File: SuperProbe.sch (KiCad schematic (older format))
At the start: 66 parts, among them J1 Conn_01x01, J10 Conn_01x01, J11 Conn_01x01, J12 Conn_01x01, J13 Conn_01x01, J14 Conn_01x01, J15 Conn_01x01, J16 Conn_01x01, J17 Conn_01x02, J2 Conn_01x01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

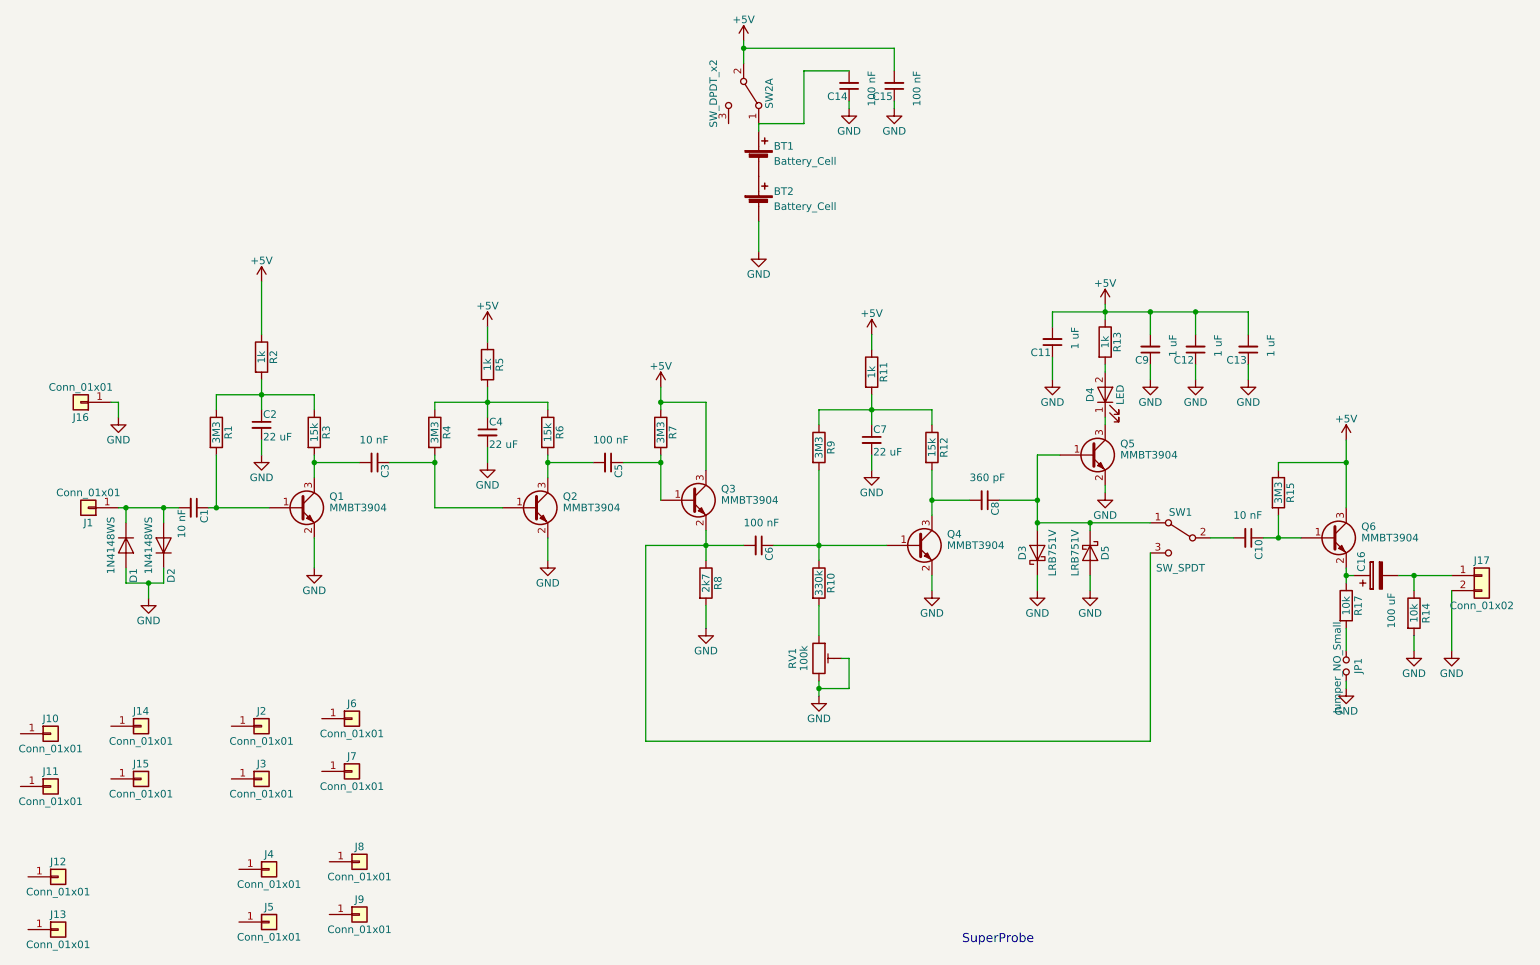
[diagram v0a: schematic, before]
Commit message: Uses 9 volt battery and board shrink
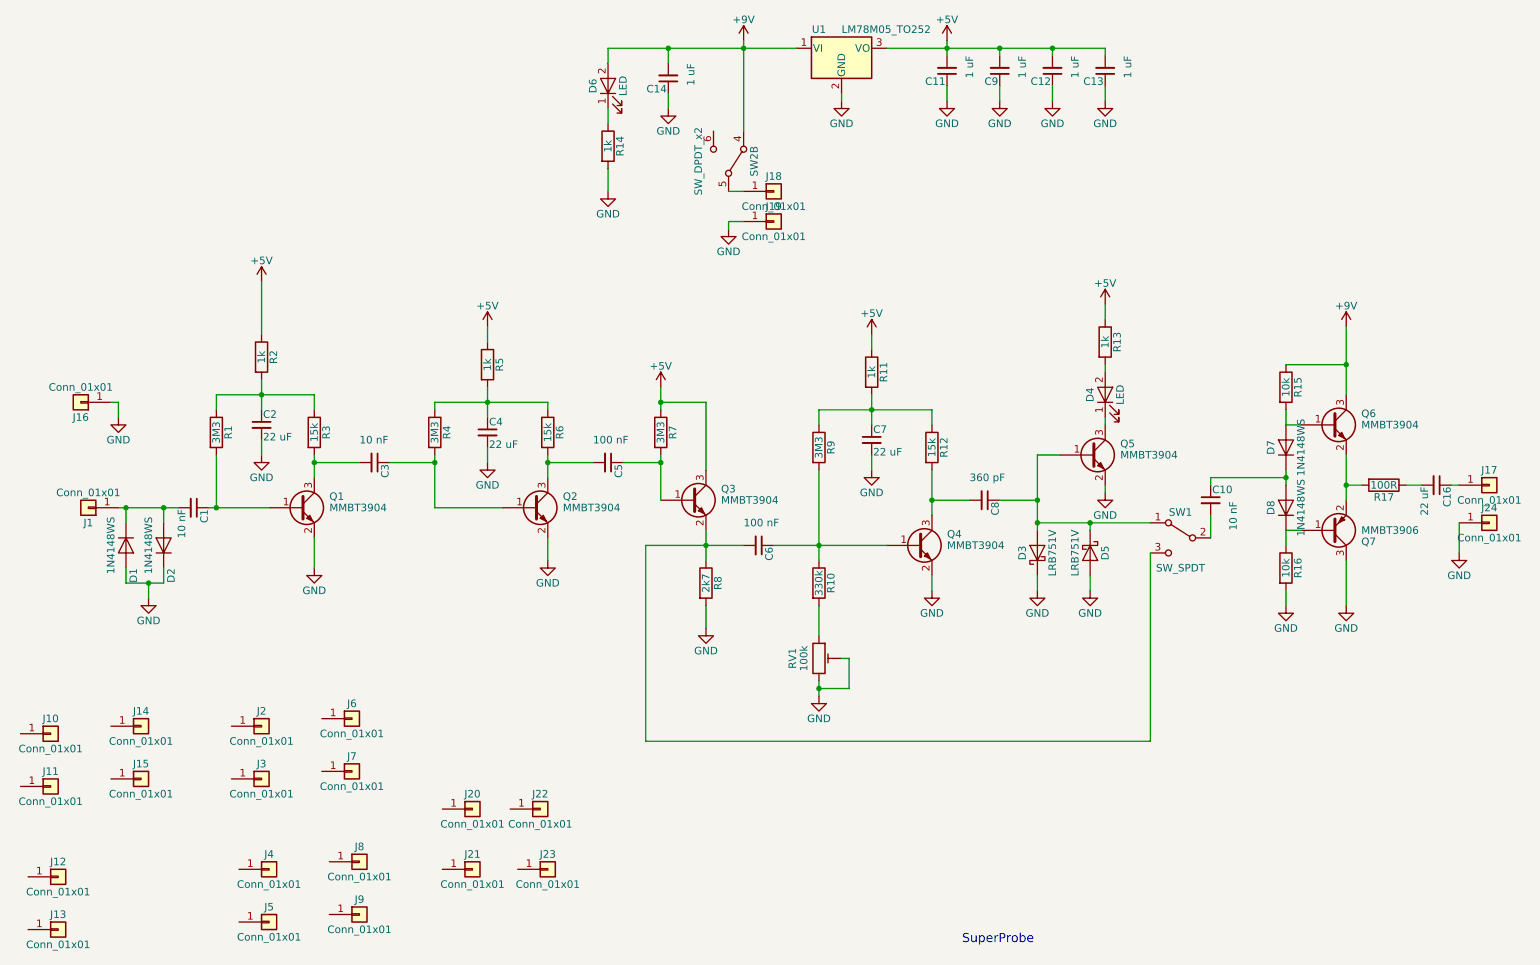
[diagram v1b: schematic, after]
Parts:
- removed BT1, BT2: Battery_Cell, Battery_Holders:Keystone_103_1x20mm-CoinCell, symbol Battery_Cell
- removed C14: 100 nF, Capacitors_SMD:C_0805_HandSoldering, symbol C_Small
- removed C16: 100 uF, Capacitors_SMD:CP_Elec_5x5.3, symbol CP
- removed J17: Conn_01x02, Connectors_Terminal_Blocks:TerminalBlock_bornier-2_P5.08mm, symbol Conn_01x02
- removed JP1: Jumper_NO_Small, Pin_Headers:Pin_Header_Straight_1x02_Pitch2.54mm, symbol Jumper_NO_Small
- removed SW2: SW_DPDT_x2, SuperProbe:DPDTsmallswitch, symbol SW_DPDT_x2
- added C16: 22 uF, Capacitors_SMD:C_1210_HandSoldering, symbol C_Small
- added D6: LED, LEDs:LED_0805_HandSoldering, symbol LED
- added D7, D8: 1N4148WS, Diodes_SMD:D_SOD-323, symbol D
- added J17, J18, J19, J24: Conn_01x01, Connectors:1pin, symbol Conn_01x01
- added J20, J21, J22, J23: Conn_01x01, SuperProbe:BigSlot, symbol Conn_01x01
- added Q7: MMBT3906, TO_SOT_Packages_SMD:SOT-23, symbol MMBT3906
- added R16: 10k, Resistors_SMD:R_0805_HandSoldering, symbol R
- added SW2: SW_DPDT_x2, SuperProbe:DPDTsmallswitch, symbol SW_DPDT_x2
- added U1: LM78M05_TO252, TO_SOT_Packages_SMD:TO-252-3_TabPin2, symbol LM78M05_TO252
- C14: renamed from C15; value 100 nF -> 1 uF
- R14: value 10k -> 1k
- R15: value 3M3 -> 10k
- R17: value 10k -> 100R
- SW1: footprint Pin_Headers:Pin_Header_Straight_1x03_Pitch2.54mm -> SuperProbe:DPDTsmallswitch
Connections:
- net +5V: now also U1.3 (VO); no longer C14.2, Q6.3 (C), R15.1
- net GND: now also J19.1 (Pin_1), J24.1 (Pin_1), Q7.3 (C), R16.2, U1.2 (GND)
- net at Q6.1 (B), R15.2: now also D7.2 (A); no longer C10.1
- net at Q6.2 (E): now also R17.2, Q7.2 (E); no longer R17.1
- net at R14.1: now also D6.1 (K)
- new net: C10.1, D7.1 (K), D8.2 (A)
- new net: J18.1 (Pin_1), SW2.5 (B)
- new net: C16.1, J17.1 (Pin_1)
- new net: C16.2, R17.1
- new net: D8.1 (K), Q7.1 (B), R16.1
- new net +9V: C14.2, D6.2 (A), Q6.3 (C), R15.1, SW2.4 (A), U1.1 (VI)
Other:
- moved on the sheet: C10, C11, C12, C13, C14, C9, Q6

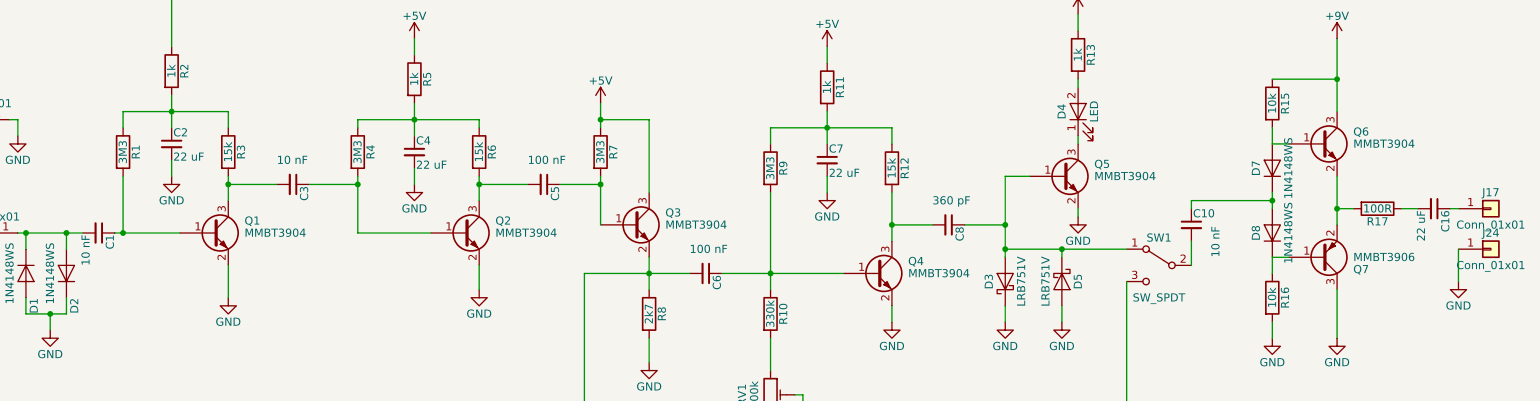
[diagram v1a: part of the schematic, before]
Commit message: Cleaned up the board slightly
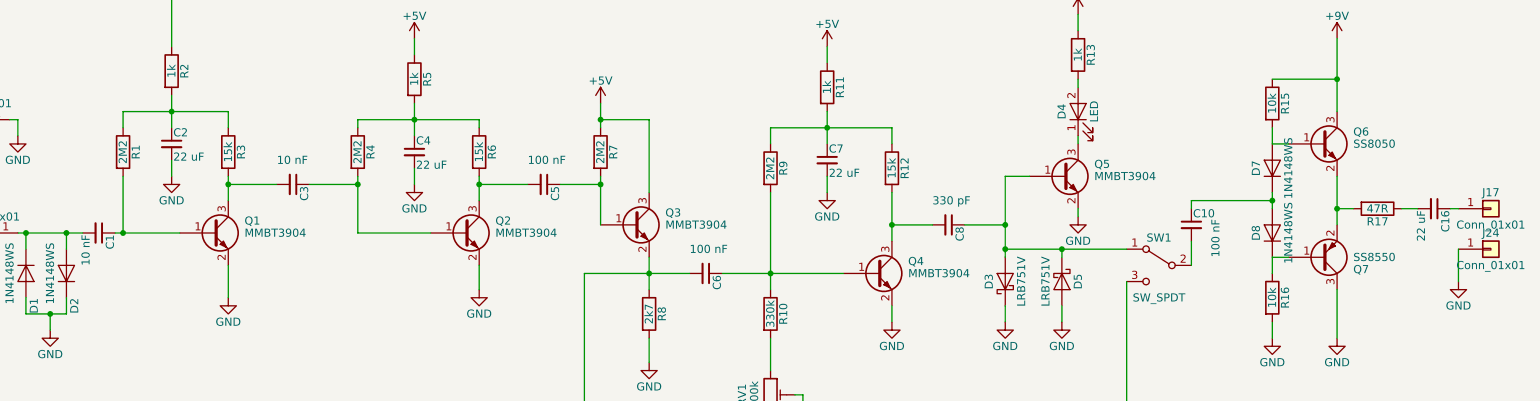
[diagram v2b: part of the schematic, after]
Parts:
- C1, C3: LCSC (none) -> C1710
- C10: value 10 nF -> 100 nF; LCSC (none) -> C49678
- C11, C12, C13, C14, C9: LCSC (none) -> C28323
- C16, C2, C4, C7: footprint Capacitors_SMD:C_1210_HandSoldering -> Capacitors_SMD:C_0805_HandSoldering; LCSC (none) -> C45783
- C5: LCSC (none) -> C49678
- C8: value 360 pF -> 330 pF; LCSC (none) -> C51207
- D1, D2, D7, D8: LCSC (none) -> C2128
- D3, D5: LCSC (none) -> C131730
- D4: LCSC (none) -> C34499
- D6: LCSC (none) -> C2296
- J1, J16, J17, J18, J19, J24: footprint Connectors:1pin -> SuperProbe:PadHole
- Q1, Q2, Q3, Q4, Q5: LCSC (none) -> C20526
- Q6: value MMBT3904 -> SS8050; LCSC (none) -> C2150
- Q7: value MMBT3906 -> SS8550; LCSC (none) -> C8542
- R1, R4, R7, R9: value 3M3 -> 2M2; LCSC (none) -> C26113
- R10: LCSC (none) -> C17629
- R11, R13, R14, R2, R5: LCSC (none) -> C17513
- R12, R3, R6: LCSC (none) -> C17475
- R15, R16: LCSC (none) -> C17414
- R17: value 100R -> 47R; LCSC (none) -> C17714
- U1: LCSC (none) -> C58069

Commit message: Eliminated unneeded diode
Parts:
- removed D3: LRB751V, Diodes_SMD:D_SOD-323_HandSoldering, symbol D_Schottky
- R17: value 47R -> 0R; LCSC C17714 -> C17477
- R8: LCSC (none) -> C17530
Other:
- moved on the sheet: D5
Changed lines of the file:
@@
 $EndComp
 $Comp
-L GND #PWR5
+L GND #PWR01
 U 1 1 5E9B90E6
 P 3200 4300
-F 0 "#PWR5" H 3200 4050 50  0001 C CNN
+F 0 "#PWR01" H 3200 4050 50  0001 C CNN
 F 1 "GND" H 3200 4150 50  0000 C CNN
 F 2 "" H 3200 4300 50  0001 C CNN
@@
 $EndComp
 $Comp
-L GND #PWR4
+L GND #PWR02
 U 1 1 5E9B912A
 P 2850 3550
-F 0 "#PWR4" H 2850 3300 50  0001 C CNN
+F 0 "#PWR02" H 2850 3300 50  0001 C CNN
 F 1 "GND" H 2850 3400 50  0000 C CNN
 F 2 "" H 2850 3550 50  0001 C CNN
@@
 $EndComp
 $Comp
-L +5V #PWR3
+L +5V #PWR03
 U 1 1 5E9B9267
 P 2850 2400
-F 0 "#PWR3" H 2850 2250 50  0001 C CNN
+F 0 "#PWR03" H 2850 2250 50  0001 C CNN
 F 1 "+5V" H 2850 2540 50  0000 C CNN
 F 2 "" H 2850 2400 50  0001 C CNN
@@
 $EndComp
 $Comp
-L GND #PWR8
+L GND #PWR04
 U 1 1 5E9B935A
 P 4750 4250
-F 0 "#PWR8" H 4750 4000 50  0001 C CNN
+F 0 "#PWR04" H 4750 4000 50  0001 C CNN
 F 1 "GND" H 4750 4100 50  0000 C CNN
 F 2 "" H 4750 4250 50  0001 C CNN
@@
 $EndComp
 $Comp
-L GND #PWR7
+L GND #PWR05
 U 1 1 5E9B968B
 P 4350 3600
-F 0 "#PWR7" H 4350 3350 50  0001 C CNN
+F 0 "#PWR05" H 4350 3350 50  0001 C CNN
 F 1 "GND" H 4350 3450 50  0000 C CNN
 F 2 "" H 4350 3600 50  0001 C CNN
@@
 $EndComp
 $Comp
-L +5V #PWR6
+L +5V #PWR06
 U 1 1 5E9B97C5
 P 4350 2700
-F 0 "#PWR6" H 4350 2550 50  0001 C CNN
+F 0 "#PWR06" H 4350 2550 50  0001 C CNN
 F 1 "+5V" H 4350 2840 50  0000 C CNN
 F 2 "" H 4350 2700 50  0001 C CNN
@@
 $EndComp
 $Comp
-L +5V #PWR10
+L +5V #PWR07
 U 1 1 5E9B9BD0
 P 5500 3100
-F 0 "#PWR10" H 5500 2950 50  0001 C CNN
+F 0 "#PWR07" H 5500 2950 50  0001 C CNN
 F 1 "+5V" H 5500 3240 50  0000 C CNN
 F 2 "" H 5500 3100 50  0001 C CNN
@@
 F 2 "Resistors_SMD:R_0805_HandSoldering" V 5730 4400 50  0001 C CNN
 F 3 "" H 5800 4400 50  0001 C CNN
+F 4 "C17530" V 5800 4400 60  0001 C CNN "LCSC"
 	1    5800 4400
 	1    0    0    -1
 $EndComp
 $Comp
-L GND #PWR12
+L GND #PWR08
 U 1 1 5E9B9E9B
 P 5800 4700
-F 0 "#PWR12" H 5800 4450 50  0001 C CNN
+F 0 "#PWR08" H 5800 4450 50  0001 C CNN
 F 1 "GND" H 5800 4550 50  0000 C CNN
 F 2 "" H 5800 4700 50  0001 C CNN
@@
 $EndComp
 $Comp
-L GND #PWR15
+L GND #PWR09
 U 1 1 5E9BA341
 P 6550 5150
-F 0 "#PWR15" H 6550 4900 50  0001 C CNN
+F 0 "#PWR09" H 6550 4900 50  0001 C CNN
 F 1 "GND" H 6550 5000 50  0000 C CNN
 F 2 "" H 6550 5150 50  0001 C CNN
@@
 $EndComp
 $Comp
-L GND #PWR18
+L GND #PWR010
 U 1 1 5E9BA5EE
 P 6900 3650
-F 0 "#PWR18" H 6900 3400 50  0001 C CNN
+F 0 "#PWR010" H 6900 3400 50  0001 C CNN
 F 1 "GND" H 6900 3500 50  0000 C CNN
 F 2 "" H 6900 3650 50  0001 C CNN
@@
 $EndComp
 $Comp
-L +5V #PWR17
+L +5V #PWR011
 U 1 1 5E9BA9B5
 P 6900 2750
-F 0 "#PWR17" H 6900 2600 50  0001 C CNN
+F 0 "#PWR011" H 6900 2600 50  0001 C CNN
 F 1 "+5V" H 6900 2890 50  0000 C CNN
 F 2 "" H 6900 2750 50  0001 C CNN
@@
 $EndComp
 $Comp
-L GND #PWR19
+L GND #PWR012
 U 1 1 5E9BACE0
 P 7300 4450
-F 0 "#PWR19" H 7300 4200 50  0001 C CNN
+F 0 "#PWR012" H 7300 4200 50  0001 C CNN
 F 1 "GND" H 7300 4300 50  0000 C CNN
 F 2 "" H 7300 4450 50  0001 C CNN
@@
 $EndComp
 $Comp
-L D_Schottky D3
-U 1 1 5E9BB050
-P 8000 4200
-F 0 "D3" H 8000 4300 50  0000 C CNN
-F 1 "LRB751V" H 8000 4100 50  0000 C CNN
-F 2 "Diodes_SMD:D_SOD-323_HandSoldering" H 8000 4200 50  0001 C CNN
-F 3 "" H 8000 4200 50  0001 C CNN
-F 4 "C131730" H 8000 4200 60  0001 C CNN "LCSC"
-	1    8000 4200
-	0    -1   -1   0
-$EndComp
-$Comp
-L GND #PWR23
-U 1 1 5E9BB166
-P 8000 4450
-F 0 "#PWR23" H 8000 4200 50  0001 C CNN
-F 1 "GND" H 8000 4300 50  0000 C CNN
-F 2 "" H 8000 4450 50  0001 C CNN
-F 3 "" H 8000 4450 50  0001 C CNN
-	1    8000 4450
-	1    0    0    -1
-$EndComp
-$Comp
 L MMBT3904 Q5
 U 1 1 5E9BB277
@@
 $EndComp
 $Comp
-L GND #PWR28
+L GND #PWR013
 U 1 1 5E9BB380
 P 8450 3800
-F 0 "#PWR28" H 8450 3550 50  0001 C CNN
+F 0 "#PWR013" H 8450 3550 50  0001 C CNN
 F 1 "GND" H 8450 3650 50  0000 C CNN
 F 2 "" H 8450 3800 50  0001 C CNN
@@
 $EndComp
 $Comp
-L +5V #PWR27
+L +5V #PWR014
 U 1 1 5E9BB7DB
 P 8450 2550
-F 0 "#PWR27" H 8450 2400 50  0001 C CNN
+F 0 "#PWR014" H 8450 2400 50  0001 C CNN
 F 1 "+5V" H 8450 2690 50  0000 C CNN
 F 2 "" H 8450 2550 50  0001 C CNN
@@
 $EndComp
 $Comp
-L GND #PWR31
+L GND #PWR015
 U 1 1 5E9BD546
 P 10050 4550
-F 0 "#PWR31" H 10050 4300 50  0001 C CNN
+F 0 "#PWR015" H 10050 4300 50  0001 C CNN
 F 1 "GND" H 10050 4400 50  0000 C CNN
 F 2 "" H 10050 4550 50  0001 C CNN
@@
 $EndComp
 $Comp
-L GND #PWR2
+L GND #PWR016
 U 1 1 5E9BF682
 P 2100 4500
-F 0 "#PWR2" H 2100 4250 50  0001 C CNN
+F 0 "#PWR016" H 2100 4250 50  0001 C CNN
 F 1 "GND" H 2100 4350 50  0000 C CNN
 F 2 "" H 2100 4500 50  0001 C CNN
@@
 $EndComp
 $Comp
-L GND #PWR13
+L GND #PWR017
 U 1 1 5E9C1122
 P 5950 2050
-F 0 "#PWR13" H 5950 1800 50  0001 C CNN
+F 0 "#PWR017" H 5950 1800 50  0001 C CNN
 F 1 "GND" H 5950 1900 50  0000 C CNN
 F 2 "" H 5950 2050 50  0001 C CNN
@@
 $EndComp
 $Comp
-L GND #PWR1
+L GND #PWR018
 U 1 1 5E9C57D4
 P 1900 3300
-F 0 "#PWR1" H 1900 3050 50  0001 C CNN
+F 0 "#PWR018" H 1900 3050 50  0001 C CNN
 F 1 "GND" H 1900 3150 50  0000 C CNN
 F 2 "" H 1900 3300 50  0001 C CNN
@@
 L D_Schottky D5
 U 1 1 5E9C8115
-P 8350 4200
-F 0 "D5" H 8350 4300 50  0000 C CNN
-F 1 "LRB751V" H 8350 4100 50  0000 C CNN
-F 2 "Diodes_SMD:D_SOD-323_HandSoldering" H 8350 4200 50  0001 C CNN
-F 3 "" H 8350 4200 50  0001 C CNN
-F 4 "C131730" H 8350 4200 60  0001 C CNN "LCSC"
-	1    8350 4200
+P 8000 4200
+F 0 "D5" H 8000 4300 50  0000 C CNN
+F 1 "LRB751V" H 8000 4100 50  0000 C CNN
+F 2 "Diodes_SMD:D_SOD-323_HandSoldering" H 8000 4200 50  0001 C CNN
+F 3 "" H 8000 4200 50  0001 C CNN
+F 4 "C131730" H 8000 4200 60  0001 C CNN "LCSC"
+	1    8000 4200
 	0    1    1    0
 $EndComp
 $Comp
-L GND #PWR25
+L GND #PWR019
 U 1 1 5E9C8204
-P 8350 4450
-F 0 "#PWR25" H 8350 4200 50  0001 C CNN
-F 1 "GND" H 8350 4300 50  0000 C CNN
-F 2 "" H 8350 4450 50  0001 C CNN
-F 3 "" H 8350 4450 50  0001 C CNN
-	1    8350 4450
+P 8000 4450
+F 0 "#PWR019" H 8000 4200 50  0001 C CNN
+F 1 "GND" H 8000 4300 50  0000 C CNN
+F 2 "" H 8000 4450 50  0001 C CNN
+F 3 "" H 8000 4450 50  0001 C CNN
+	1    8000 4450
 	1    0    0    -1
 $EndComp
@@
 $EndComp
 $Comp
-L +9V #PWR30
+L +9V #PWR020
 U 1 1 5E9C8FE7
 P 10050 2700
-F 0 "#PWR30" H 10050 2550 50  0001 C CNN
+F 0 "#PWR020" H 10050 2550 50  0001 C CNN
 F 1 "+9V" H 10050 2840 50  0000 C CNN
 F 2 "" H 10050 2700 50  0001 C CNN
@@
 $EndComp
 $Comp
-L +9V #PWR14
+L +9V #PWR021
 U 1 1 5E9C9102
 P 6050 800
-F 0 "#PWR14" H 6050 650 50  0001 C CNN
+F 0 "#PWR021" H 6050 650 50  0001 C CNN
 F 1 "+9V" H 6050 940 50  0000 C CNN
 F 2 "" H 6050 800 50  0001 C CNN
@@
 $EndComp
 $Comp
-L GND #PWR11
+L GND #PWR022
 U 1 1 5E9C9570
 P 5550 1250
-F 0 "#PWR11" H 5550 1000 50  0001 C CNN
+F 0 "#PWR022" H 5550 1000 50  0001 C CNN
 F 1 "GND" H 5550 1100 50  0000 C CNN
 F 2 "" H 5550 1250 50  0001 C CNN
@@
 $EndComp
 $Comp
-L GND #PWR16
+L GND #PWR023
 U 1 1 5E9CAB9C
 P 6700 1200
-F 0 "#PWR16" H 6700 950 50  0001 C CNN
+F 0 "#PWR023" H 6700 950 50  0001 C CNN
 F 1 "GND" H 6700 1050 50  0000 C CNN
 F 2 "" H 6700 1200 50  0001 C CNN
@@
 $EndComp
 $Comp
-L +5V #PWR20
+L +5V #PWR024
 U 1 1 5E9CAFF7
 P 7400 800
-F 0 "#PWR20" H 7400 650 50  0001 C CNN
+F 0 "#PWR024" H 7400 650 50  0001 C CNN
 F 1 "+5V" H 7400 940 50  0000 C CNN
 F 2 "" H 7400 800 50  0001 C CNN
@@
 $EndComp
 $Comp
-L GND #PWR21
+L GND #PWR025
 U 1 1 5E9CB8EC
 P 7400 1200
-F 0 "#PWR21" H 7400 950 50  0001 C CNN
+F 0 "#PWR025" H 7400 950 50  0001 C CNN
 F 1 "GND" H 7400 1050 50  0000 C CNN
 F 2 "" H 7400 1200 50  0001 C CNN
@@
 $EndComp
 $Comp
-L GND #PWR22
+L GND #PWR026
 U 1 1 5E9CB9C3
 P 7750 1200
-F 0 "#PWR22" H 7750 950 50  0001 C CNN
+F 0 "#PWR026" H 7750 950 50  0001 C CNN
 F 1 "GND" H 7750 1050 50  0000 C CNN
 F 2 "" H 7750 1200 50  0001 C CNN
@@
 $EndComp
 $Comp
-L GND #PWR24
+L GND #PWR027
 U 1 1 5E9CBA9A
 P 8100 1200
-F 0 "#PWR24" H 8100 950 50  0001 C CNN
+F 0 "#PWR027" H 8100 950 50  0001 C CNN
 F 1 "GND" H 8100 1050 50  0000 C CNN
 F 2 "" H 8100 1200 50  0001 C CNN
@@
 $EndComp
 $Comp
-L GND #PWR26
+L GND #PWR028
 U 1 1 5E9CBEDE
 P 8450 1200
-F 0 "#PWR26" H 8450 950 50  0001 C CNN
+F 0 "#PWR028" H 8450 950 50  0001 C CNN
 F 1 "GND" H 8450 1050 50  0000 C CNN
 F 2 "" H 8450 1200 50  0001 C CNN
@@
 $EndComp
 $Comp
-L GND #PWR29
+L GND #PWR029
 U 1 1 5E9CE6A4
 P 9650 4550
-F 0 "#PWR29" H 9650 4300 50  0001 C CNN
+F 0 "#PWR029" H 9650 4300 50  0001 C CNN
 F 1 "GND" H 9650 4400 50  0000 C CNN
 F 2 "" H 9650 4550 50  0001 C CNN
@@
 Connection ~ 7300 3850
 Wire Wire Line
-	8000 4450 8000 4350
-Wire Wire Line
 	8000 3550 8000 4050
 Wire Wire Line
@@
 Connection ~ 6050 850
 Wire Wire Line
-	8350 4450 8350 4350
-Wire Wire Line
-	8350 4050 8350 4000
-Connection ~ 8350 4000
+	8000 4450 8000 4350
 Wire Wire Line
 	10050 4250 10050 4550
@@
 Connection ~ 10050 3750
 $Comp
-L GND #PWR32
+L GND #PWR030
 U 1 1 5E9CF183
 P 10800 4200
-F 0 "#PWR32" H 10800 3950 50  0001 C CNN
+F 0 "#PWR030" H 10800 3950 50  0001 C CNN
 F 1 "GND" H 10800 4050 50  0000 C CNN
 F 2 "" H 10800 4200 50  0001 C CNN
@@
 P 10300 3750
 F 0 "R17" V 10380 3750 50  0000 C CNN
-F 1 "47R" V 10300 3750 50  0000 C CNN
+F 1 "0R" V 10300 3750 50  0000 C CNN
 F 2 "Resistors_SMD:R_0805_HandSoldering" V 10230 3750 50  0001 C CNN
 F 3 "" H 10300 3750 50  0001 C CNN
-F 4 "C17714" V 10300 3750 60  0001 C CNN "LCSC"
+F 4 "C17477" V 10300 3750 60  0001 C CNN "LCSC"
 	1    10300 3750
 	0    1    1    0
@@
 $EndComp
 $Comp
-L GND #PWR9
+L GND #PWR031
 U 1 1 5E9CFF23
 P 5150 1800
-F 0 "#PWR9" H 5150 1550 50  0001 C CNN
+F 0 "#PWR031" H 5150 1550 50  0001 C CNN
 F 1 "GND" H 5150 1650 50  0000 C CNN
 F 2 "" H 5150 1800 50  0001 C CNN
